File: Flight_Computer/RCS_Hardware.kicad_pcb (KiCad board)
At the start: 2 copper layers, 110 x 110 mm, 72 parts, among them J1 SWD, J10 Motor, J2 TYPE-C-31-M-12, J3 I2C, J4 5V, J5 GND, J6 AMT102, J7 FC_RF, J9 AMT102, Q1 2N7002, Q2 2N7002, Q3 2N7002, Q5 2N7002, Q6 2N7002, Q7 2N7002, U1 STM32F401CCU6, U2 AMS1117-3.3, U3 TMP102xxDRL, U4 BNO055, U5 W25Q32JVSS, U6 LM2576S-5, Y1 16MHz, Y2 32.768Mhz

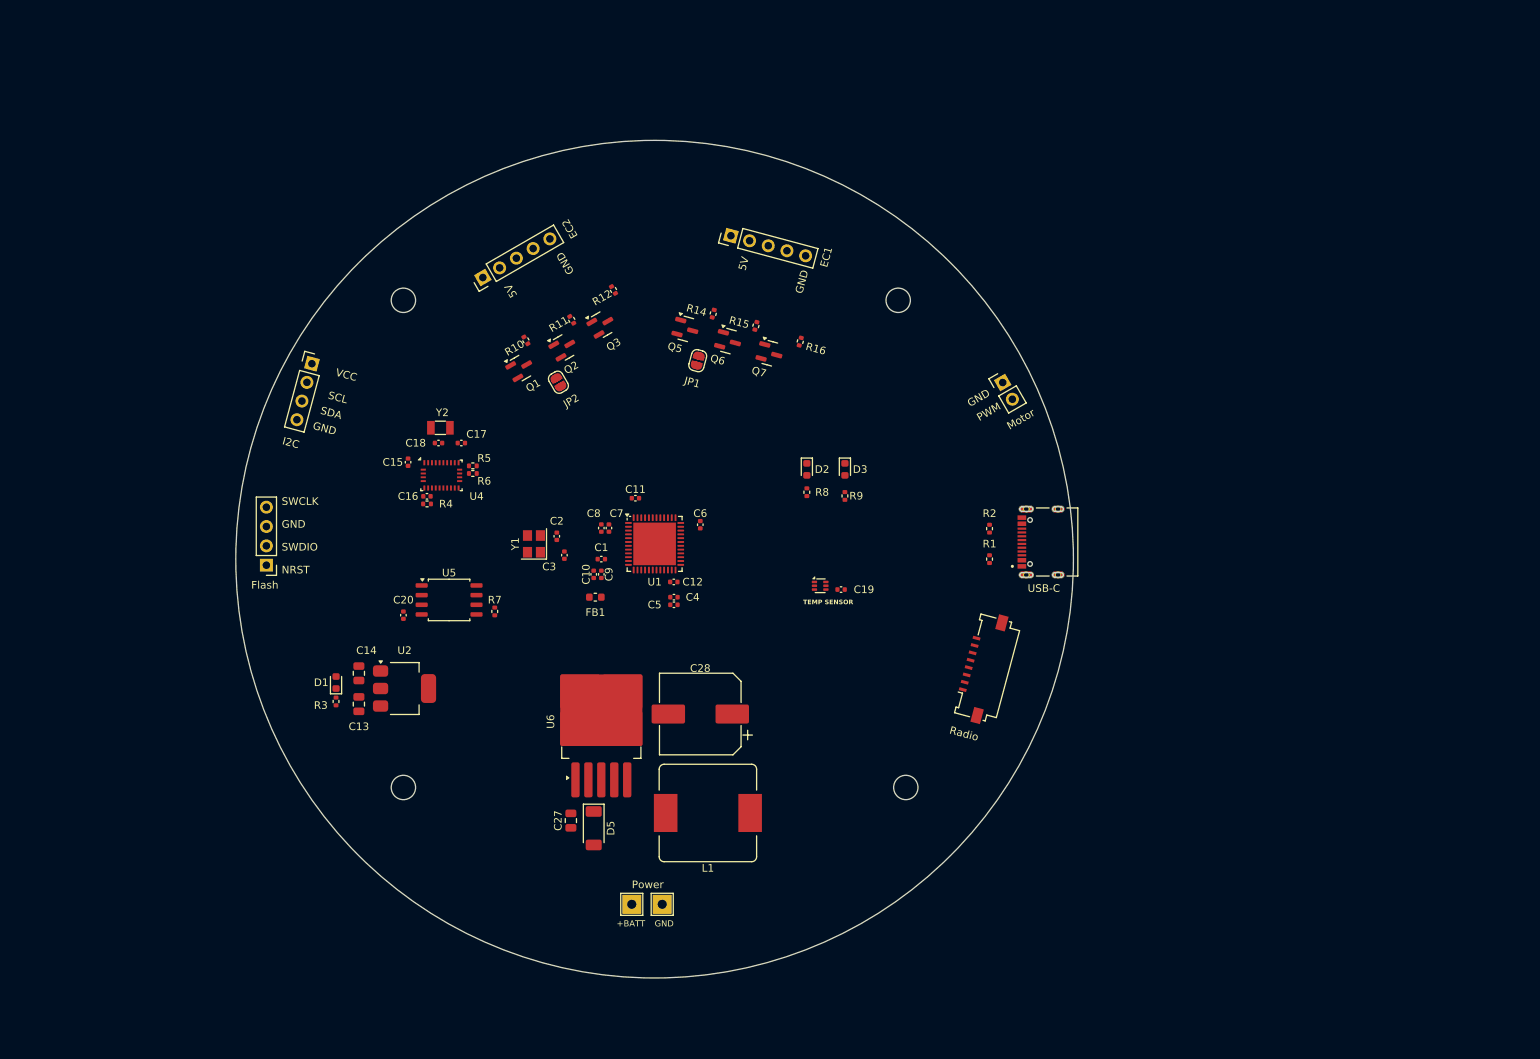
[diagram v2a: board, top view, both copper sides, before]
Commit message: routed most of pcb and updated encoder level-shifting circuit
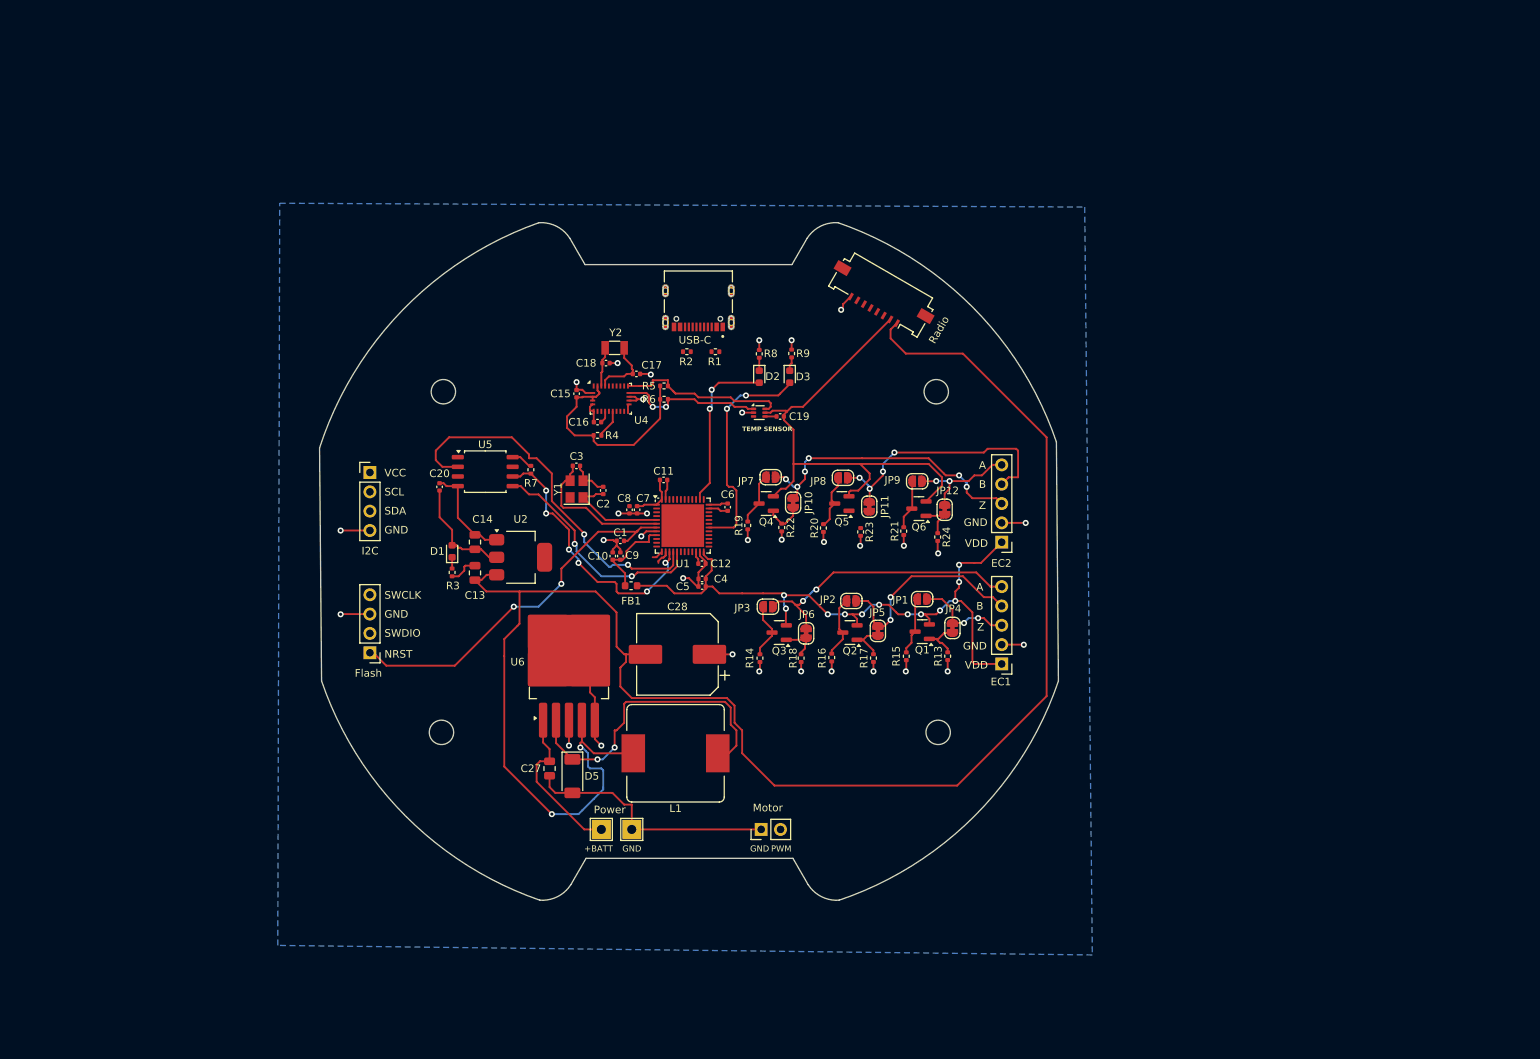
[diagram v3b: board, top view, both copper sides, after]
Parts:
- removed J9: AMT102, Connector_PinHeader_2.54mm:PinHeader_1x05_P2.54mm_Vertical
- removed Q7: 2N7002, Package_TO_SOT_SMD:SOT-23
- removed R10, R11, R12: 1k, Resistor_SMD:R_0402_1005Metric
- added G***: LOGO, LOGO, B.Cu at (143.7, 95.6)
- added J8: AMT102, Connector_PinHeader_2.54mm:PinHeader_1x05_P2.54mm_Vertical, F.Cu at (185.6, 97.8)
- added JP10: SolderJumper_2_Bridged, Jumper:SolderJumper-2_P1.3mm_Bridged_RoundedPad1.0x1.5mm, F.Cu at (158.2, 92.6)
- added JP11: SolderJumper_2_Bridged, Jumper:SolderJumper-2_P1.3mm_Bridged_RoundedPad1.0x1.5mm, F.Cu at (168.2, 93.1)
- added JP12: SolderJumper_2_Bridged, Jumper:SolderJumper-2_P1.3mm_Bridged_RoundedPad1.0x1.5mm, F.Cu at (178.1, 93.5)
- added JP3: SolderJumper_2_Open, Jumper:SolderJumper-2_P1.3mm_Open_RoundedPad1.0x1.5mm, F.Cu at (154.9, 106.2)
- added JP4: SolderJumper_2_Bridged, Jumper:SolderJumper-2_P1.3mm_Bridged_RoundedPad1.0x1.5mm, F.Cu at (179.1, 109.0)
- added JP5: SolderJumper_2_Bridged, Jumper:SolderJumper-2_P1.3mm_Bridged_RoundedPad1.0x1.5mm, F.Cu at (169.3, 109.4)
- added JP6: SolderJumper_2_Bridged, Jumper:SolderJumper-2_P1.3mm_Bridged_RoundedPad1.0x1.5mm, F.Cu at (159.9, 109.8)
- added JP7: SolderJumper_2_Open, Jumper:SolderJumper-2_P1.3mm_Open_RoundedPad1.0x1.5mm, F.Cu at (155.2, 89.2)
- added JP8: SolderJumper_2_Open, Jumper:SolderJumper-2_P1.3mm_Open_RoundedPad1.0x1.5mm, F.Cu at (164.7, 89.3)
- added JP9: SolderJumper_2_Open, Jumper:SolderJumper-2_P1.3mm_Open_RoundedPad1.0x1.5mm, F.Cu at (174.5, 89.8)
- added Q4: 2N7002, Package_TO_SOT_SMD:SOT-23, F.Cu at (154.7, 92.7)
- added R13: 1K, Resistor_SMD:R_0402_1005Metric, F.Cu at (178.5, 112.8)
- added R17: 1K, Resistor_SMD:R_0402_1005Metric, F.Cu at (168.8, 113.0)
- added R18: 1K, Resistor_SMD:R_0402_1005Metric, F.Cu at (159.2, 113.0)
- added R19: 1k, Resistor_SMD:R_0402_1005Metric, F.Cu at (152.2, 95.6)
- added R20: 1K, Resistor_SMD:R_0402_1005Metric, F.Cu at (162.2, 95.9)
- added R21: 1k, Resistor_SMD:R_0402_1005Metric, F.Cu at (172.7, 96.3)
- added R22: 1K, Resistor_SMD:R_0402_1005Metric, F.Cu at (156.7, 95.8)
- added R23: 1K, Resistor_SMD:R_0402_1005Metric, F.Cu at (167.1, 96.4)
- added R24: 1K, Resistor_SMD:R_0402_1005Metric, F.Cu at (177.2, 97.1)
- R16: value 1k -> 1K
- moved H3 80.0 mm to (112.2, 78.0)
- moved H1 71.0 mm to (177.0, 78.0)
- moved J10 66.7 mm to (154.0, 135.5), turned to 90 degrees
- moved J6 66.6 mm to (185.6, 113.8), turned to 180 degrees
- moved Q1 63.1 mm to (175.2, 109.5), turned to 180 degrees
- moved J2 57.6 mm to (145.8, 64.8), turned to 180 degrees
- moved H2 57.0 mm to (177.2, 122.8)
- moved Q2 53.1 mm to (165.7, 109.6), turned to 180 degrees
- moved J7 49.3 mm to (169.3, 66.5), turned to 150 degrees
- moved JP2 48.0 mm to (165.9, 105.5), turned to 180 degrees
- moved R15 47.7 mm to (173.1, 112.8), turned to 90 degrees
- moved Q3 46.7 mm to (156.4, 109.7), turned to 180 degrees
- moved R2 46.1 mm to (144.2, 72.8), turned to 0 degrees
- moved R14 45.7 mm to (153.8, 113.0), turned to 90 degrees
- moved R1 45.2 mm to (148.0, 72.8), turned to 180 degrees
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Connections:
- J6 pad 1: Net-(J6-Pin_1) -> +3.3V
- J6 pad 2: +5V -> GND
- J6 pad 5: GND -> Net-(J6-Pin_5)
- JP1 pad 2: Net-(J6-Pin_1) -> /E1Z
- JP2 pad 1: Net-(J9-Pin_3) -> Net-(J6-Pin_4)
- JP2 pad 2: Net-(J9-Pin_1) -> /E1B
- Q1 pad 1: Net-(J9-Pin_1) -> Net-(JP4-B)
- Q1 pad 3: /E2B -> /E1Z
- Q2 pad 3: /I2 -> /E1B
- Q3 pad 1: Net-(J9-Pin_3) -> Net-(JP6-B)
- Q3 pad 3: /E2A -> /E1A
- Q5 pad 1: Net-(J6-Pin_1) -> Net-(JP11-B)
- Q5 pad 3: /E1B -> /E2B
- Q6 pad 1: Net-(J6-Pin_3) -> Net-(JP12-B)
- Q6 pad 3: /E1A -> /E2A
- R14 pad 2: /E1B -> /E1A
- R15 pad 2: /E1A -> /E1Z
- R16 pad 2: /I1 -> /E1B
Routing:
- net +5V: track 0.00 -> 229.8 mm, vias 0 -> 2
- net +3.3V: track 0.00 -> 204.5 mm, vias 0 -> 12
- net GND: track 0.00 -> 146.0 mm, vias 0 -> 32
- net /NRST: track 0.00 -> 49.4 mm, vias 0 -> 2
- net /MISO: track 0.00 -> 48.8 mm, vias 0 -> 2
- net Net-(D5-K): track 0.00 -> 41.2 mm, vias 0 -> 2
- net Net-(J8-Pin_3): track 0.00 -> 38.0 mm, vias 0 -> 6
- net Net-(J6-Pin_5): track 0.00 -> 36.7 mm, vias 0 -> 2
- net /SCLK: track 0.00 -> 35.6 mm, vias 0 -> 6
- net Net-(J8-Pin_4): track 0.00 -> 34.0 mm, vias 0 -> 4
- net /MOSI: track 0.00 -> 30.4 mm, vias 0 -> 2
- net /LED_B: track 0.00 -> 29.6 mm, vias 0 -> 2
- net Net-(J6-Pin_4): track 0.00 -> 27.7 mm, vias 0 -> 2
- net /SDA: track 0.00 -> 22.4 mm
- net /LED_G: track 0.00 -> 21.7 mm, vias 0 -> 2
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- added copper zone on B.Cu, net GND
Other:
- board size 110 x 110 mm -> 97.1 x 89 mm
- board text added: "A"
- board text added: "B"
- board text added: "VDD"
- board text added: "Z"
- board text removed: "5V"

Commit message: updated gyro schematic and started placing PCB
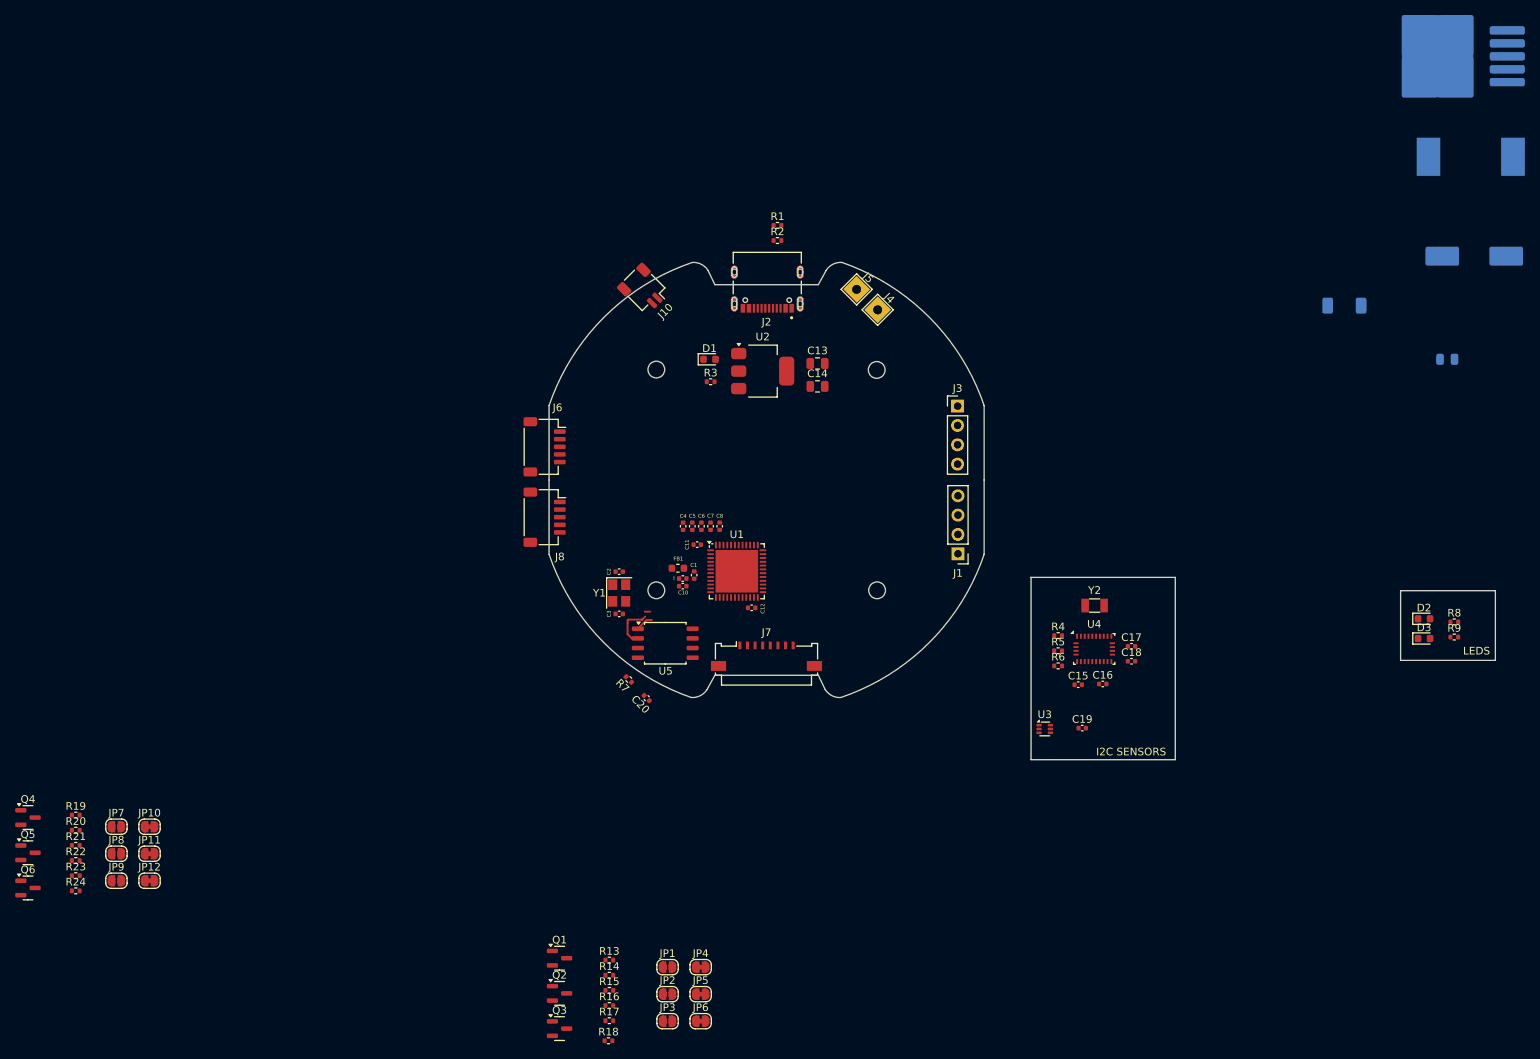
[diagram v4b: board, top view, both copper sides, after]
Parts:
- C27, C28, D5, L1, U6: moved to B.Cu
- H1, H2, H3, H4: footprint MountingHole:MountingHole_3.2mm_M3 -> MountingHole:MountingHole_2.2mm_M2
- J10: footprint Connector_PinHeader_2.54mm:PinHeader_1x02_P2.54mm_Vertical -> Connector_JST:JST_SH_SM02B-SRSS-TB_1x02-1MP_P1.00mm_Horizontal
- J6, J8: footprint Connector_PinHeader_2.54mm:PinHeader_1x05_P2.54mm_Vertical -> Connector_JST:JST_SH_SM05B-SRSS-TB_1x05-1MP_P1.00mm_Horizontal
- moved G*** 180.5 mm to (322.6, 72.1)
- moved U6 140.3 mm to (244.4, 34.0), turned to 180 degrees
- moved L1 130.6 mm to (247.2, 47.1)
- moved C27 129.6 mm to (244.1, 73.8), turned to 180 degrees
- moved Q6 127.2 mm to (57.7, 143.2), turned to 0 degrees
- moved R24 122.4 mm to (64.0, 143.6), turned to 0 degrees
- moved D5 118.8 mm to (230.6, 66.7), turned to 180 degrees
- moved JP9 117.6 mm to (69.3, 142.2), turned to 0 degrees
- moved C28 117.0 mm to (247.7, 60.2)
- moved Q5 116.3 mm to (57.7, 138.6), turned to 0 degrees
- moved R21 116.3 mm to (64.0, 137.6), turned to 0 degrees
- moved JP12 115.3 mm to (73.7, 142.2), turned to 0 degrees
- moved R23 112.6 mm to (64.0, 141.6), turned to 0 degrees
- moved JP8 107.5 mm to (69.3, 138.7), turned to 0 degrees
- moved R20 105.9 mm to (64.0, 135.6), turned to 0 degrees
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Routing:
- net +5V: track 229.8 -> 0.00 mm, vias 2 -> 0
- net +3.3V: track 204.5 -> 0.00 mm, vias 12 -> 0
- net GND: track 146.0 -> 0.00 mm, vias 32 -> 0
- net /NRST: track 49.4 -> 0.00 mm, vias 2 -> 0
- net /MISO: track 48.8 -> 6.65 mm, vias 2 -> 0
- net Net-(D5-K): track 41.2 -> 0.00 mm, vias 2 -> 0
- net Net-(J8-Pin_3): track 38.0 -> 0.00 mm, vias 6 -> 0
- net Net-(J6-Pin_5): track 36.7 -> 0.00 mm, vias 2 -> 0
- net /SCLK: track 35.6 -> 0.00 mm, vias 6 -> 0
- net Net-(J8-Pin_4): track 34.0 -> 0.00 mm, vias 4 -> 0
- net /MOSI: track 30.4 -> 0.00 mm, vias 2 -> 0
- net /LED_B: track 29.6 -> 0.00 mm, vias 2 -> 0
- net Net-(J6-Pin_4): track 27.7 -> 0.00 mm, vias 2 -> 0
- net /SDA: track 22.4 -> 0.00 mm
- net /LED_G: track 21.7 -> 0.00 mm, vias 2 -> 0
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- removed copper zone on B.Cu, net GND
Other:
- board size 97.1 x 89 mm -> 124.3 x 65.3 mm
- board text added: "C1"
- board text added: "C10"
- board text added: "C11"
- board text added: "C2"
- board text added: "C3"
- board text added: "C4"
- board text added: "C5"
- board text added: "C6"
- board text added: "C8"
- board text added: "C9"
- board text added: "FB1"
- board text added: "I2C SENSORS"
- board text added: "LEDS"
- board text removed: "+BATT"
- board text removed: "A"
- board text removed: "B"
- board text removed: "EC1"
- board text removed: "EC2"
- board text removed: "Flash"
- board text removed: "GND"
- board text removed: "I2C"
- board text removed: "Motor"
- board text removed: "NRST"
- board text removed: "PWM"
- board text removed: "Power"
- board text removed: "Radio"
- board text removed: "SCL"
- board text removed: "SDA"
- board text removed: "SWCLK"
- board text removed: "SWDIO"
- board text removed: "TEMP SENSOR"
- board text removed: "USB-C"
- board text removed: "VCC"
- board text removed: "VDD"
- board text removed: "Z"
